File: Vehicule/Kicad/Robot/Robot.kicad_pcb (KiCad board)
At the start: 2 copper layers, 60 x 50 mm, 10 parts, among them J2 Conn_01x02_Socket_H, J3 Conn_01x02_Socket_H, J4 Conn_01x02_Socket_H, J5 Conn_01x02_Socket_H, SW1 SW_DPDT_x2, U1 ESP32-C3_SUPERMINI, U2 L293D, U4 REG_5V

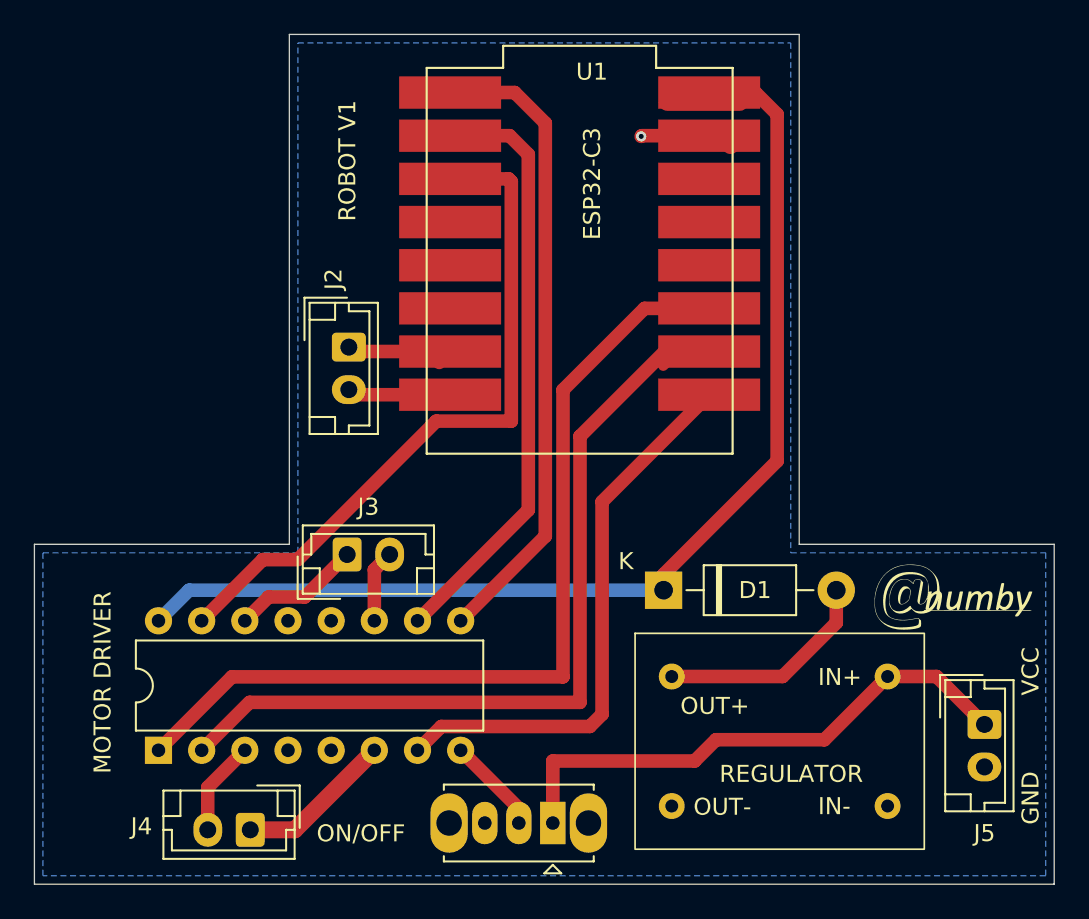
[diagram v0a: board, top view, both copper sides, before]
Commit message: Remplacement de l'empreinte ESP32 de surface pour une empreinte traversante
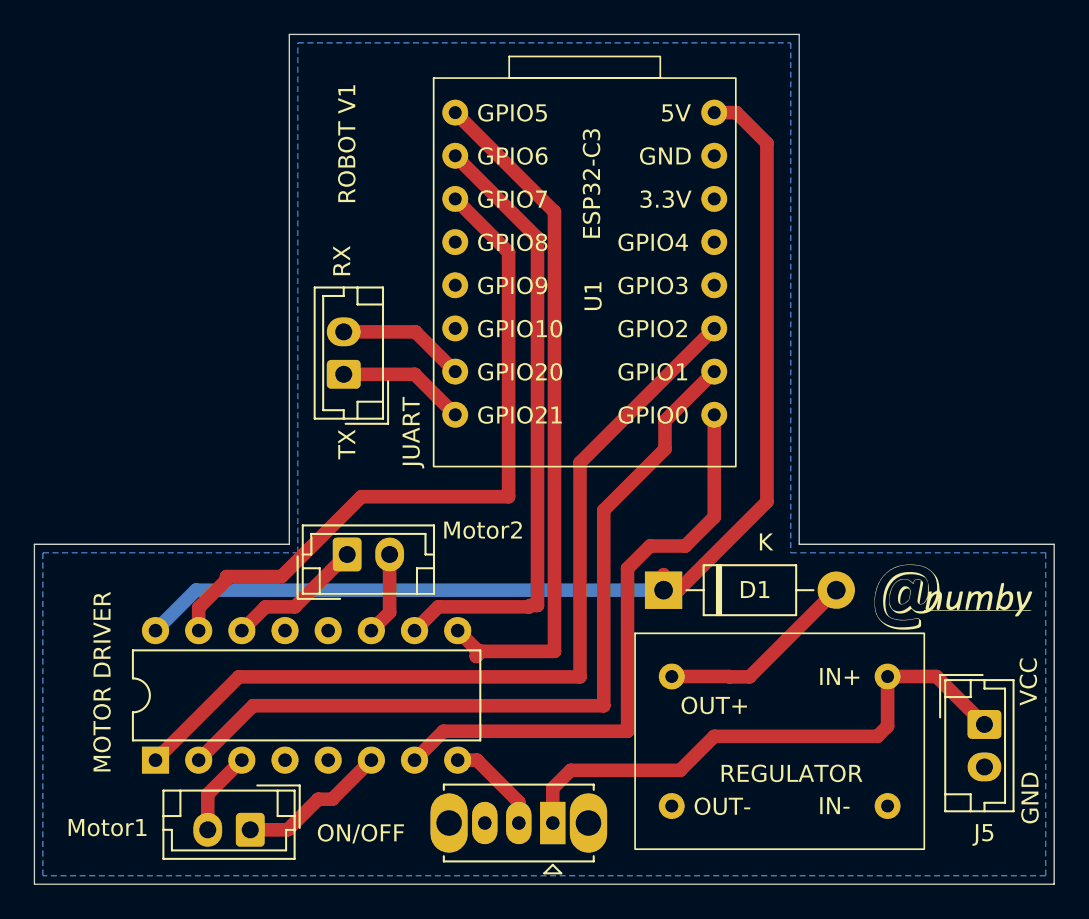
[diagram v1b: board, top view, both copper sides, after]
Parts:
- U1: value ESP32-C3_SUPERMINI -> ~; footprint Anumby:ESP32-C3-SUPERMINI -> Anumby:ESP32-C3_SUPERMINI
- moved JUART 1.63 mm to (90.3, 122.9), turned to 90 degrees
- moved U2 0.61 mm to (79.2, 145.6)
- moved U1 0.34 mm to (104.5, 116.4)
- renumbered J2 to JUART, J4 to Motor1, J3 to Motor2
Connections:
- U1 pad 1: Net-(U1-GPIO1) -> Net-(D1-K)
- U1 pad 10: unconnected-(U1-GPIO10-Pad10) -> Net-(J2-Pin_2)
- U1 pad 2: Net-(U1-GPIO2) -> GND
- U1 pad 5: Net-(U1-GPIO5) -> unconnected-(U1-GPIO3-Pad5)
- U1 pad 6: Net-(U1-GPIO6) -> Net-(U1-GPIO2)
- U1 pad 7: Net-(U1-GPIO7) -> Net-(U1-GPIO1)
- U1 pad 8: unconnected-(U1-GPIO8-Pad8) -> Net-(U1-GPIO0)
- U1 pad 9: unconnected-(U1-GPIO9-Pad9) -> Net-(J2-Pin_1)
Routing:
- net Net-(D1-K): track 70.2 -> 65.0 mm
- net GND: track 4.21 -> 0.14 mm, vias 1 -> 0
- net Net-(U1-GPIO2): track 53.3 -> 50.8 mm
- net Net-(U1-GPIO0): track 33.1 -> 35.2 mm
- net Net-(U1-GPIO7): track 43.3 -> 41.2 mm
- net Net-(U1-GPIO1): track 49.1 -> 47.5 mm
- net Net-(J2-Pin_2): track 6.11 -> 7.53 mm
- net Net-(U1-GPIO6): track 37.6 -> 36.3 mm
- net Net-(D1-A): track 12.9 -> 11.8 mm
- net Net-(J5-Pin_1): track 32.3 -> 33.0 mm
- net Net-(J3-Pin_2): track 4.27 -> 4.93 mm
- net Net-(J4-Pin_2): track 5.58 -> 4.93 mm
- net Net-(J2-Pin_1): track 7.00 -> 7.55 mm
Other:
- board text added: "Motor2"
- board text added: "RX"
- board text added: "TX"

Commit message: Modification des fichiers Kicad de Gilles Premier test de la gestion de l'historique du trajet Chris/robot.py
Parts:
- renumbered JUART to UART
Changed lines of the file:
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@@
 		(descr "JST EH series connector, B2B-EH-A (http://www.jst-mfg.com/product/pdf/eng/eEH.pdf), generated with kicad-footprint-generator")
 		(tags "connector JST EH vertical")
-		(property "Reference" "JUART"
+		(property "Reference" "UART"
 			(at -3.4 4 90)
 			(layer "F.SilkS")
